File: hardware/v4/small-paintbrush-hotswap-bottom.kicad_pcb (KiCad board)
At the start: 2 copper layers, 94 x 47 mm, 4 parts

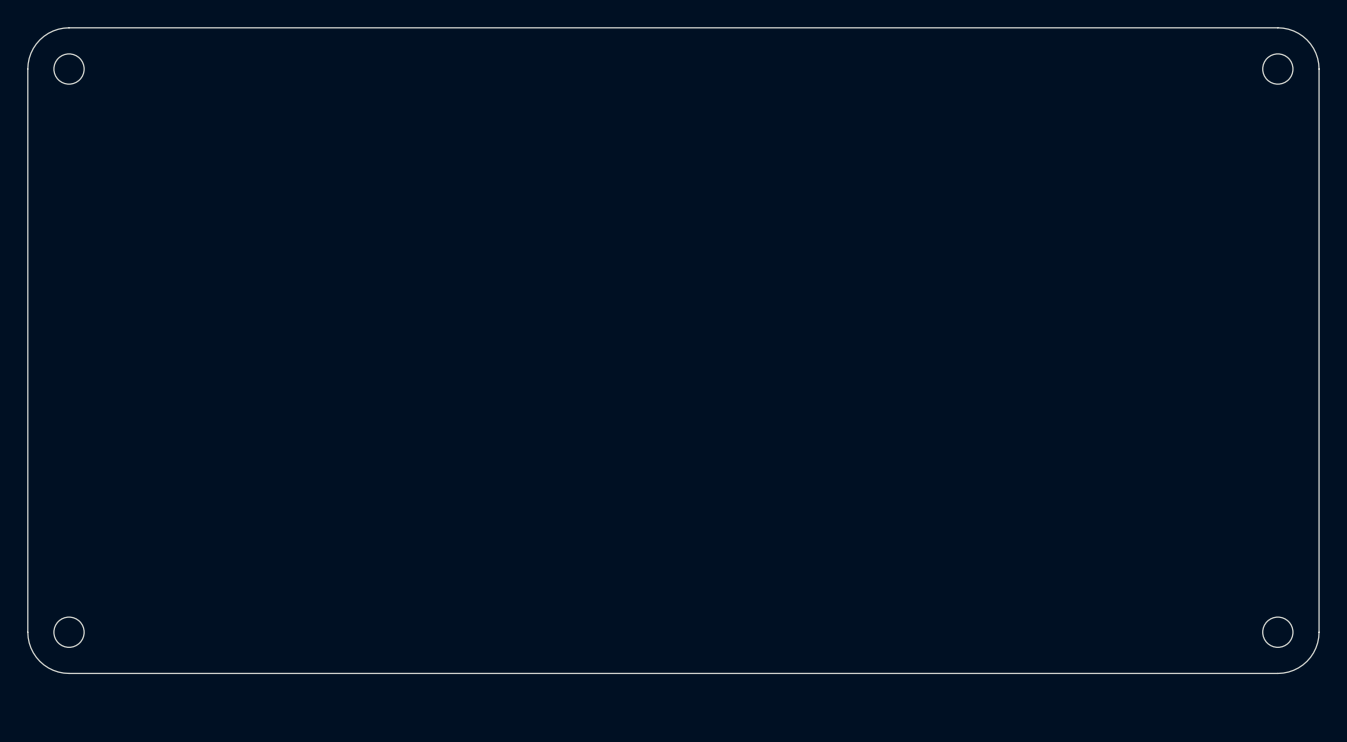
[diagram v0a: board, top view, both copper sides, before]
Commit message: Remove unnecessary files ; fix v4 bottom plate size
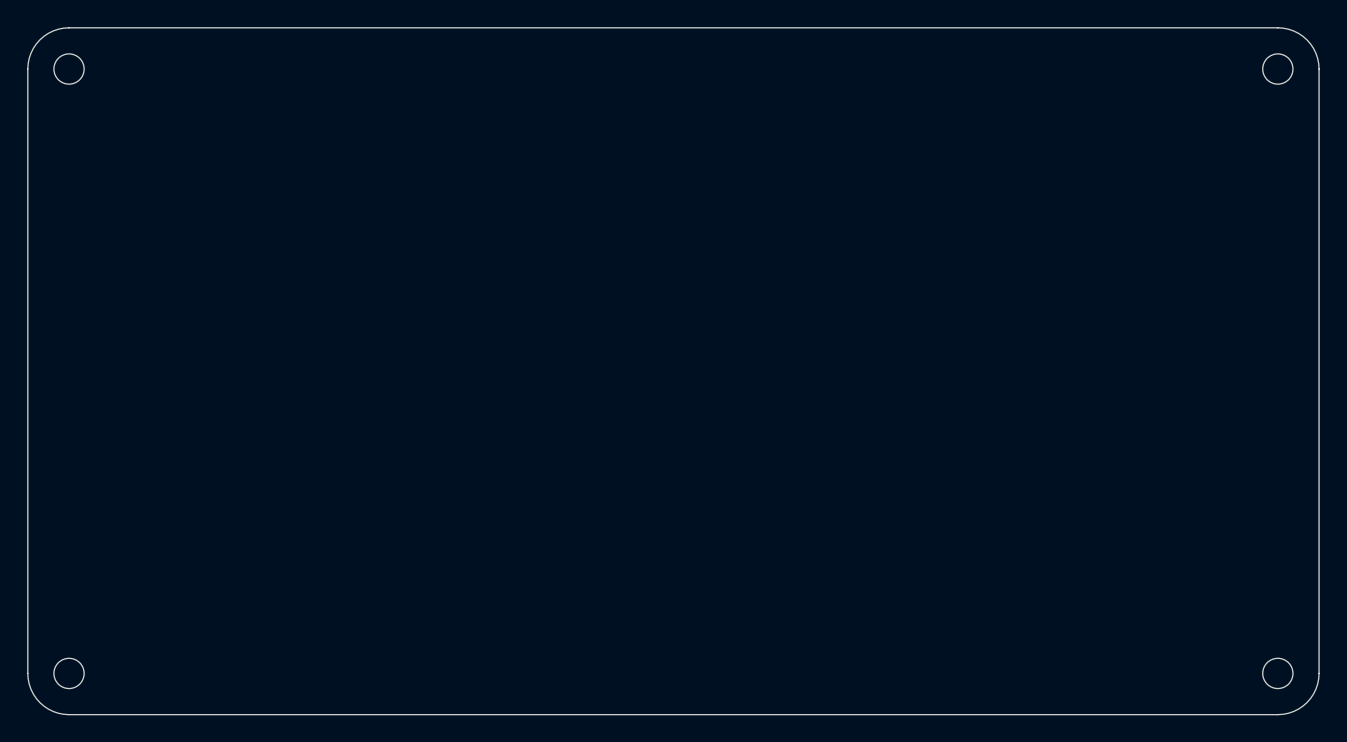
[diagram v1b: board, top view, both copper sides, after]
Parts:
- moved REF** 3.00 mm to (78.9, 65.6)
- moved REF** 3.00 mm to (166.9, 65.6)
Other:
- board size 94 x 47 mm -> 94 x 50 mm
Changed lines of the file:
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@@
   )
   (module MountingHole:MountingHole_2.2mm_M2 (layer F.Cu)
-    (at 78.901739 62.599424)
+    (at 78.901739 65.599424)
+    (descr "Mounting Hole 2.2mm, no annular, M2")
+    (tags "mounting hole 2.2mm no annular m2")
+    (attr virtual)
+    (fp_text reference REF** (at 0 -3.2) (layer F.SilkS) hide
+      (effects (font (size 1 1) (thickness 0.15)))
+    )
+    (fp_text value MountingHole_2.2mm_M2 (at 0 3.2) (layer F.Fab)
+      (effects (font (size 1 1) (thickness 0.15)))
+    )
+    (fp_circle (center 0 0) (end 2.45 0) (layer F.CrtYd) (width 0.05))
+    (fp_circle (center 0 0) (end 2.2 0) (layer Cmts.User) (width 0.15))
+    (fp_text user %R (at 0.3 0) (layer F.Fab)
+      (effects (font (size 1 1) (thickness 0.15)))
+    )
+    (pad 1 np_thru_hole circle (at 0 0) (size 2.2 2.2) (drill 2.2) (layers *.Cu *.Mask))
+  )
+  (module MountingHole:MountingHole_2.2mm_M2 (layer F.Cu)
+    (at 78.901736 21.599424)
     (descr "Mounting Hole 2.2mm, no annular, M2")
     (tags "mounting hole 2.2mm no annular m2")
@@
   )
   (module MountingHole:MountingHole_2.2mm_M2 (layer F.Cu)
-    (at 78.901736 21.599424)
+    (at 166.901739 65.599426)
     (descr "Mounting Hole 2.2mm, no annular, M2")
     (tags "mounting hole 2.2mm no annular m2")
@@
       (effects (font (size 1 1) (thickness 0.15)))
     )
+    (fp_circle (center 0 0) (end 2.2 0) (layer Cmts.User) (width 0.15))
     (fp_circle (center 0 0) (end 2.45 0) (layer F.CrtYd) (width 0.05))
-    (fp_circle (center 0 0) (end 2.2 0) (layer Cmts.User) (width 0.15))
-    (fp_text user %R (at 0.3 0) (layer F.Fab)
-      (effects (font (size 1 1) (thickness 0.15)))
-    )
-    (pad 1 np_thru_hole circle (at 0 0) (size 2.2 2.2) (drill 2.2) (layers *.Cu *.Mask))
-  )
-  (module MountingHole:MountingHole_2.2mm_M2 (layer F.Cu)
-    (at 166.901739 62.599426)
-    (descr "Mounting Hole 2.2mm, no annular, M2")
-    (tags "mounting hole 2.2mm no annular m2")
-    (attr virtual)
-    (fp_text reference REF** (at 0 -3.2) (layer F.SilkS) hide
-      (effects (font (size 1 1) (thickness 0.15)))
-    )
-    (fp_text value MountingHole_2.2mm_M2 (at 0 3.2) (layer F.Fab)
-      (effects (font (size 1 1) (thickness 0.15)))
-    )
-    (fp_circle (center 0 0) (end 2.45 0) (layer F.CrtYd) (width 0.05))
-    (fp_circle (center 0 0) (end 2.2 0) (layer Cmts.User) (width 0.15))
     (fp_text user %R (at 0.3 0) (layer F.Fab)
       (effects (font (size 1 1) (thickness 0.15)))
@@
       (effects (font (size 1 1) (thickness 0.15)))
     )
+    (fp_circle (center 0 0) (end 2.2 0) (layer Cmts.User) (width 0.15))
     (fp_circle (center 0 0) (end 2.45 0) (layer F.CrtYd) (width 0.05))
-    (fp_circle (center 0 0) (end 2.2 0) (layer Cmts.User) (width 0.15))
     (fp_text user %R (at 0.3 0) (layer F.Fab)
       (effects (font (size 1 1) (thickness 0.15)))
@@
     (pad 1 np_thru_hole circle (at 0 0) (size 2.2 2.2) (drill 2.2) (layers *.Cu *.Mask))
   )
-  (gr_arc (start 78.901739 62.599424) (end 75.901739 62.599426) (angle -90) (layer Edge.Cuts) (width 0.05))
-  (gr_line (start 166.901737 65.599424) (end 78.901736 65.599424) (layer Edge.Cuts) (width 0.05))
+  (gr_arc (start 78.901739 65.599424) (end 75.901739 65.599426) (angle -90) (layer Edge.Cuts) (width 0.05))
+  (gr_line (start 166.901737 68.599424) (end 78.901736 68.599424) (layer Edge.Cuts) (width 0.05))
   (gr_arc (start 166.901737 21.599424) (end 169.901739 21.599423) (angle -90) (layer Edge.Cuts) (width 0.05))
   (gr_line (start 78.901738 18.599424) (end 166.901737 18.599423) (layer Edge.Cuts) (width 0.05))
   (gr_arc (start 78.901736 21.599424) (end 78.901738 18.599424) (angle -90) (layer Edge.Cuts) (width 0.05))
-  (gr_arc (start 166.901739 62.599426) (end 166.901737 65.599424) (angle -90) (layer Edge.Cuts) (width 0.05))
-  (gr_line (start 75.901739 62.599426) (end 75.901738 21.599424) (layer Edge.Cuts) (width 0.05))
-  (gr_line (start 169.901739 21.599423) (end 169.901739 62.599424) (layer Edge.Cuts) (width 0.05))
+  (gr_arc (start 166.901739 65.599426) (end 166.901737 68.599424) (angle -90) (layer Edge.Cuts) (width 0.05))
+  (gr_line (start 75.901739 65.599426) (end 75.901736 21.599422) (layer Edge.Cuts) (width 0.05))
+  (gr_line (start 169.901739 21.599423) (end 169.901737 65.599428) (layer Edge.Cuts) (width 0.05))
 )
